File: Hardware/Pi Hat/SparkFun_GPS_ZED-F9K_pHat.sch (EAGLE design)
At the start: 88 parts, among them J1 QWIIC_RIGHT_ANGLE, J2 RASPBERRYPI-40-PIN-GPIO_SMD_S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, J4 U.FL, U1 UBLOX_ZED_F9R, U2 HCPL-270L

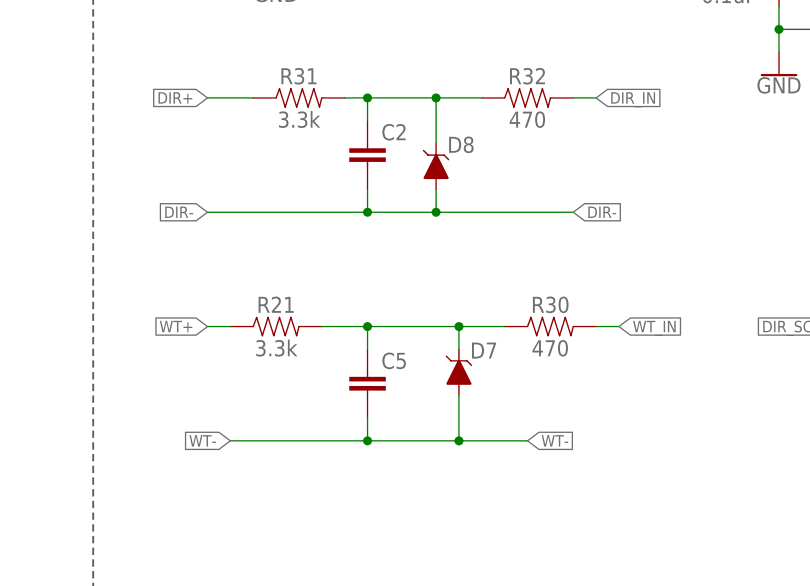
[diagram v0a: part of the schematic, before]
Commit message: Updates designs with new X7R capacitors
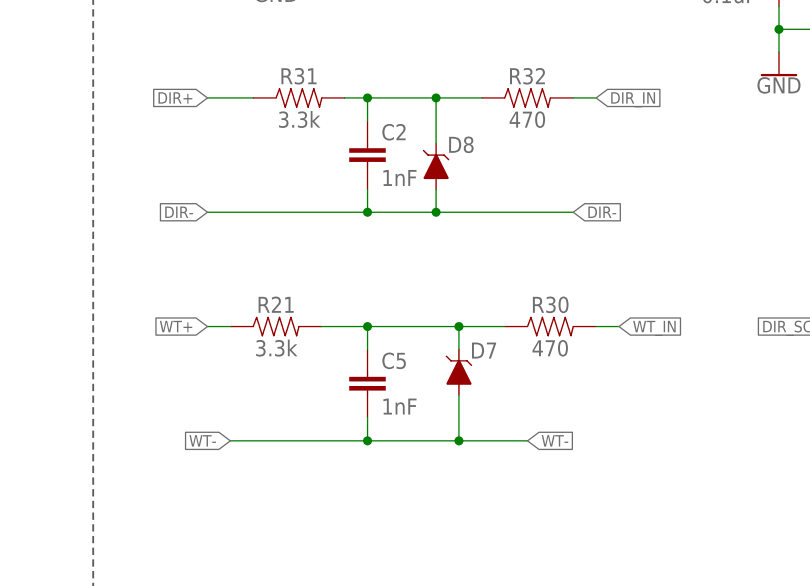
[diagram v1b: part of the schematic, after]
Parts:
- C1: device SparkFun-Capacitors:47PF-0603-50V-5% -> SparkFun-Capacitors:47PF-0402-25V-5%-X7R
- C2, C5: value 1.0nF -> 1nF; device SparkFun-Capacitors:1.0NF/1000PF-0402-50V-10% -> SparkFun-Capacitors:1.0NF/1000PF-0402-25V-10%-X7R
- C3, C4: device SparkFun-Capacitors:22NF/22,000PF-0603-50V-10% -> SparkFun-Capacitors:22NF/22,000PF-0603-25V-10%-X7R
- C7, C8, C9: device SparkFun-Capacitors:0.1UF-0402-16V-10% -> SparkFun-Capacitors:0.1UF-0402-6.3V-10%-X7R
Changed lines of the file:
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@@
 <part name="U1" library="classified" deviceset="UBLOX_ZED_F9R" device=""/>
 <part name="FRAME2" library="SparkFun-Aesthetics" deviceset="FRAME-LEDGER" device=""/>
-<part name="C1" library="SparkFun-Capacitors" deviceset="47PF" device="-0603-50V-5%" value="47pF"/>
+<part name="C1" library="SparkFun-Capacitors" deviceset="47PF" device="-0402-25V-5%-X7R" value="47pF"/>
 <part name="C6" library="SparkFun-Capacitors" deviceset="1.0UF" device="-0402-16V-10%" value="1.0uF"/>
 <part name="D4" library="SparkFun-IC-Power" deviceset="PRTR5V0U2" device="F"/>
@@
 <part name="R31" library="SparkFun-Resistors" deviceset="3.3KOHM" device="-0603-1/10W-1%" value="3.3k"/>
 <part name="R32" library="SparkFun-Resistors" deviceset="470OHM" device="-0603-1/10W-1%" value="470"/>
-<part name="C2" library="SparkFun-Capacitors" deviceset="1.0NF/1000PF" device="-0402-50V-10%" value="1.0nF"/>
-<part name="C3" library="SparkFun-Capacitors" deviceset="22NF/22,000PF" device="-0603-50V-10%" value="22nF"/>
-<part name="C4" library="SparkFun-Capacitors" deviceset="22NF/22,000PF" device="-0603-50V-10%" value="22nF"/>
-<part name="C5" library="SparkFun-Capacitors" deviceset="1.0NF/1000PF" device="-0402-50V-10%" value="1.0nF"/>
+<part name="C2" library="SparkFun-Capacitors" deviceset="1.0NF/1000PF" device="-0402-25V-10%-X7R" value="1nF"/>
+<part name="C3" library="SparkFun-Capacitors" deviceset="22NF/22,000PF" device="-0603-25V-10%-X7R" value="22nF"/>
+<part name="C4" library="SparkFun-Capacitors" deviceset="22NF/22,000PF" device="-0603-25V-10%-X7R" value="22nF"/>
+<part name="C5" library="SparkFun-Capacitors" deviceset="1.0NF/1000PF" device="-0402-25V-10%-X7R" value="1nF"/>
 <part name="D7" library="classified" deviceset="BZX84_DIODE" device="" value="0.5A/40V/420mV"/>
 <part name="R33" library="classified" deviceset="910OHM-0603-1/10W-5%" device="" value="910"/>
 <part name="R34" library="classified" deviceset="910OHM-0603-1/10W-5%" device="" value="910"/>
 <part name="U2" library="classified" deviceset="HCPL-270L" device=""/>
-<part name="C7" library="SparkFun-Capacitors" deviceset="0.1UF" device="-0402-16V-10%" value="0.1uF"/>
+<part name="C7" library="SparkFun-Capacitors" deviceset="0.1UF" device="-0402-6.3V-10%-X7R" value="0.1uF"/>
 <part name="SUPPLY9" library="SparkFun-PowerSymbols" deviceset="3.3V" device=""/>
 <part name="GND11" library="SparkFun-PowerSymbols" deviceset="GND" device=""/>
@@
 <part name="SUPPLY12" library="SparkFun-PowerSymbols" deviceset="3.3V" device=""/>
 <part name="SUPPLY13" library="SparkFun-PowerSymbols" deviceset="3.3V" device=""/>
-<part name="C8" library="SparkFun-Capacitors" deviceset="0.1UF" device="-0402-16V-10%" value="0.1uF"/>
-<part name="C9" library="SparkFun-Capacitors" deviceset="0.1UF" device="-0402-16V-10%" value="0.1uF"/>
+<part name="C8" library="SparkFun-Capacitors" deviceset="0.1UF" device="-0402-6.3V-10%-X7R" value="0.1uF"/>
+<part name="C9" library="SparkFun-Capacitors" deviceset="0.1UF" device="-0402-6.3V-10%-X7R" value="0.1uF"/>
 <part name="GND21" library="SparkFun-PowerSymbols" deviceset="GND" device=""/>
 <part name="TP6" library="SparkFun-Connectors" deviceset="TEST-POINT" device="3X4" value="TEST-POINT3X4"/>
@@
 <instance part="C2" gate="G$1" x="327.66" y="182.88" smashed="yes">
 <attribute name="NAME" x="329.184" y="185.801" size="1.778" layer="95" font="vector"/>
+<attribute name="VALUE" x="329.184" y="180.721" size="1.778" layer="96" font="vector"/>
 </instance>
 <instance part="C3" gate="G$1" x="419.1" y="157.48" smashed="yes">
@@
 <instance part="C5" gate="G$1" x="327.66" y="157.48" smashed="yes">
 <attribute name="NAME" x="329.184" y="160.401" size="1.778" layer="95" font="vector"/>
+<attribute name="VALUE" x="329.184" y="155.321" size="1.778" layer="96" font="vector"/>
 </instance>
 <instance part="D7" gate="G$1" x="337.82" y="160.02" smashed="yes" rot="R90">

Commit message: Removes gerbers, removes caps from schmitt trigger on both designs, adds 1uF cap to V_USB on breakout
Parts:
- removed C3, C4: 22nF, SparkFun-Capacitors:22NF/22,000PF-0603-25V-10%-X7R
- FB1: value FERRITE_BEAD-120_OHM-0402 -> 120NH; device SparkFun-Coils:FERRITE_BEAD-120_OHM-0402 -> SparkFun-Coils:FERRITE_BEAD_GNSS
- R5: value 10 -> 33; device SparkFun-Resistors:10OHM-0603-1/10W-1% -> SparkFun-Resistors:33OHM-0603-1/10W-1%
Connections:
- net DIR_SCHMITT: no longer C4.1
- net GND: no longer C3.2, C4.2
- net WT_SCHMITT: no longer C3.1
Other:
- moved on the sheet: C7, R33, R34, U2

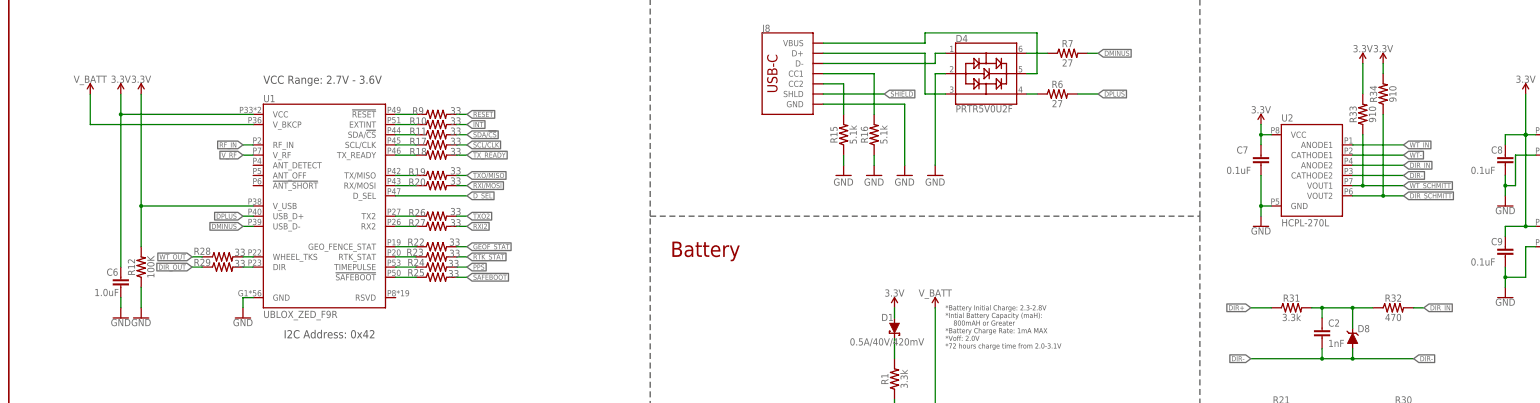
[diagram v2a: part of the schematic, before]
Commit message: Adds 1uF Cap to V_USB line
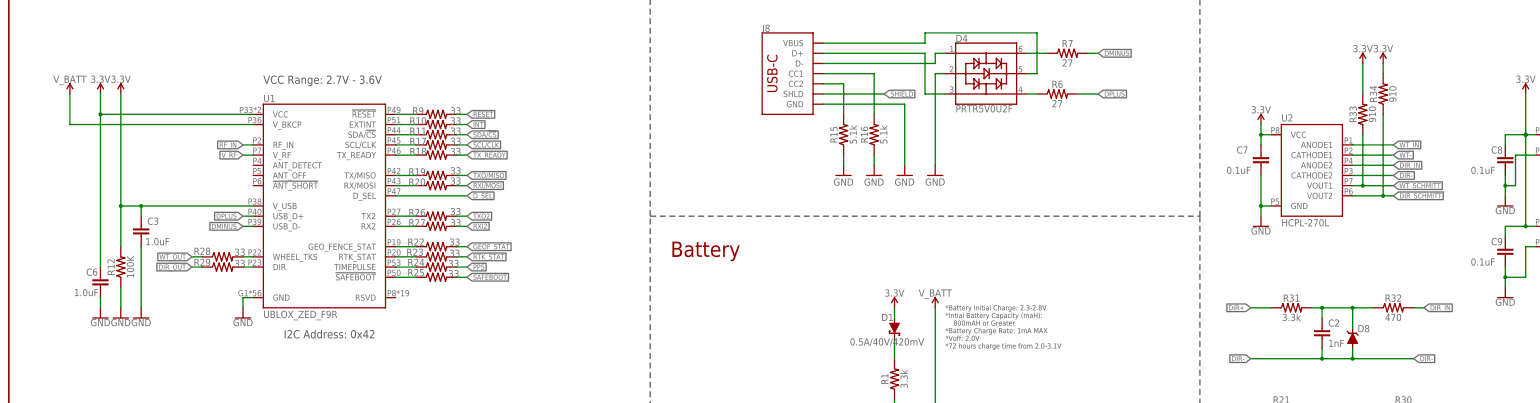
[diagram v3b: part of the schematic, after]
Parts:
- added C3: 1.0uF, SparkFun-Capacitors:1.0UF-0402-16V-10%
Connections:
- net 3.3V: now also C3.1
- net GND: now also C3.2
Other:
- moved on the sheet: C6, R12

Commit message: Updates wheel tick and direction circuitry with correct grounding
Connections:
- removed net DIR-: C2.2, D8.A, J3.9, U2.CATHODE2
- removed net GP5: J2.GP5
- removed net WT-: C5.2, D7.A, J3.7, U2.CATHODE1
- net GND: now also C2.2, C5.2, D7.A, D8.A, J3.7, J3.9, U2.CATHODE1, U2.CATHODE2
- net TX_READY: now also J2.GP5; no longer J3.1
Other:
- note added: "These nets connect the top and bottom connector together."
- note added: "These nets connect the top and bottom connectors together."
- note removed: "Nets are not routed to anything but instead routed the two 40 pin connectors to each other."
- moved on the sheet: C8, C9, D8, J3, U$30, U$31
